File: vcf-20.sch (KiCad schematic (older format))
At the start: 51 parts, among them J1 IN1, J2 IN2, J3 POWER, J4 HP, J5 LP, J6 BP, J7 NOTCH, U1 TL072, U2 LM13700, U3 TL074, U4 TL074, U9 LM4040C5

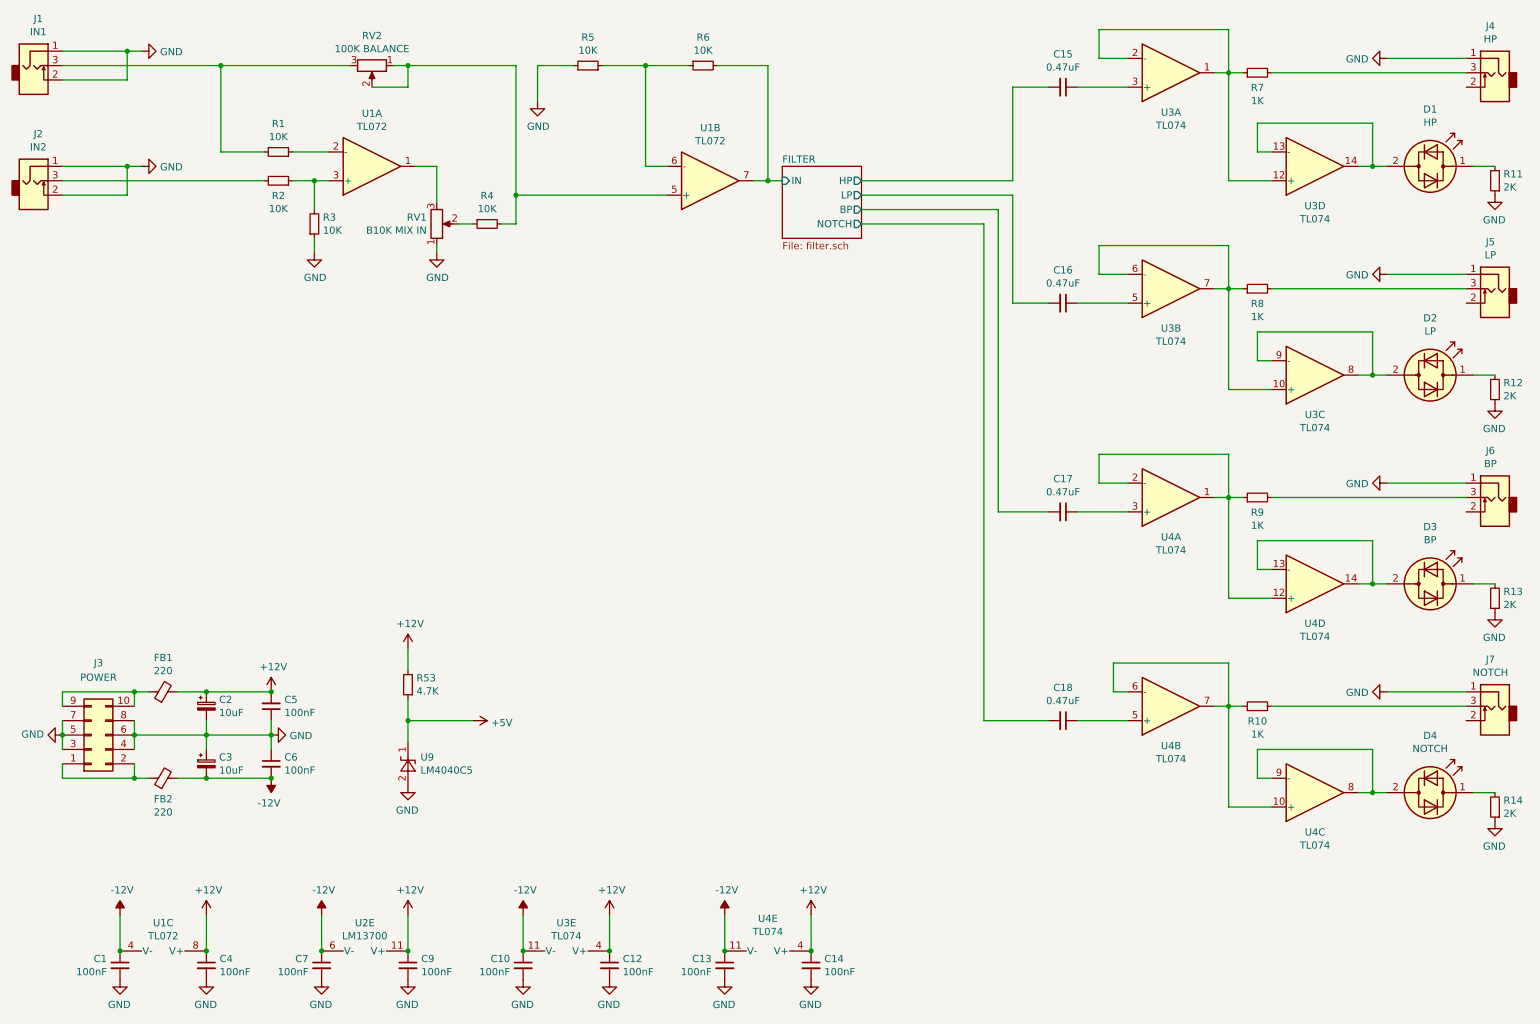
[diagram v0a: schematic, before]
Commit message: Update schematic with resonance and crossfader fixes
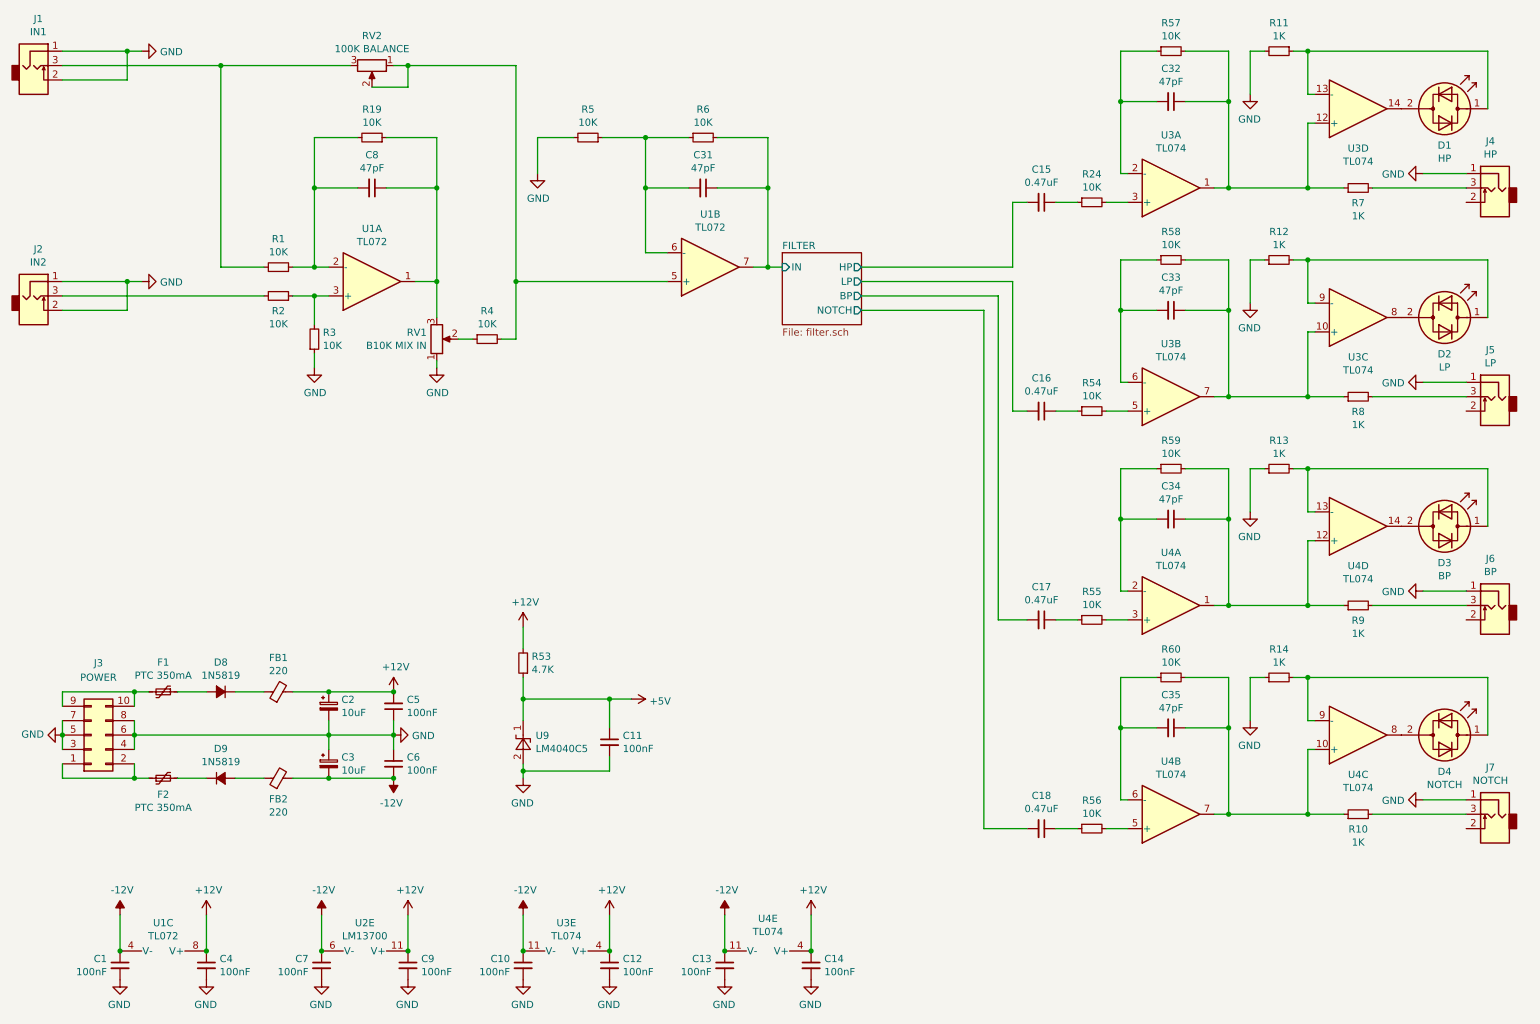
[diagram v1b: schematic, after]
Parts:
- added C11: 100nF, Capacitor_SMD:C_0603_1608Metric, symbol Device:C_Small
- added C31, C32, C33, C34, C35, C8: 47pF, Capacitor_SMD:C_0603_1608Metric, symbol Device:C_Small
- added D8, D9: 1N5819, symbol Device:D_Small_ALT
- added F1, F2: PTC 350mA, symbol Device:Polyfuse_Small
- added R19, R24, R54, R55, R56, R57, R58, R59, R60: 10K, Resistor_SMD:R_0603_1608Metric, symbol Device:R_Small
- R11, R12, R13, R14: value 2K -> 1K
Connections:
- net +5V: now also C11.1
- net FILTER/IN: now also C31.1
- net GND: now also R11.2, C11.2; no longer R11.1
- net at D1.1 (KA): now also R11.1, U3.13 (-); no longer R11.2
- net at D1.2 (AK), U3.14: no longer U3.13 (-)
- net at R7.1, U3.1, U3.12 (+): now also C32.1, R57.2; no longer U3.2 (-)
- net at J3.1 (Pin_1), J3.2 (Pin_2): now also F2.1; no longer FB2.1
- net at J3.10 (Pin_10), J3.9 (Pin_9): now also F1.2; no longer FB1.1
- net at U3.3 (+): now also R24.2; no longer C15.1
- net at R5.1, R6.1, U1.6 (-): now also C31.2
- net at D2.1 (KA), R12.2: now also U3.9 (-)
- net at D2.2 (AK), U3.8: no longer U3.9 (-)
- net at R8.1, U3.10 (+), U3.7: now also C33.1, R58.2; no longer U3.6 (-)
- net at U3.5 (+): now also R54.2; no longer C16.1
- net at D3.1 (KA), R13.2: now also U4.13 (-)
- net at D3.2 (AK), U4.14: no longer U4.13 (-)
- net at R9.1, U4.1, U4.12 (+): now also C34.1, R59.2; no longer U4.2 (-)
- net at U4.3 (+): now also R55.2; no longer C17.1
- net at R10.1, U4.10 (+), U4.7: now also C35.1, R60.2; no longer U4.6 (-)
- net at U4.5 (+): now also R56.2; no longer C18.1
- net at D4.1 (KA), R14.2: now also U4.9 (-)
- net at D4.2 (AK), U4.8: no longer U4.9 (-)
- net at RV1.3, U1.1: now also C8.1, R19.1
- net at R1.1, U1.2 (-): now also C8.2, R19.2
- new net: D8.1 (K), FB1.1
- new net: D9.2 (A), FB2.1
- new net: C32.2, R57.1, U3.2 (-)
- new net: C33.2, R58.1, U3.6 (-)
- new net: C34.2, R59.1, U4.2 (-)
- new net: C35.2, R60.1, U4.6 (-)
- new net: C17.1, R55.1
- new net: C16.1, R54.1
- new net: C15.1, R24.1
- new net: C18.1, R56.1
- new net: D8.2 (A), F1.1
- new net: D9.1 (K), F2.2
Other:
- moved on the sheet: C15, C16, C17, C18, C2, C3, C5, C6, D1, D2, D3, D4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

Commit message: Redesign filter core and revise board layout
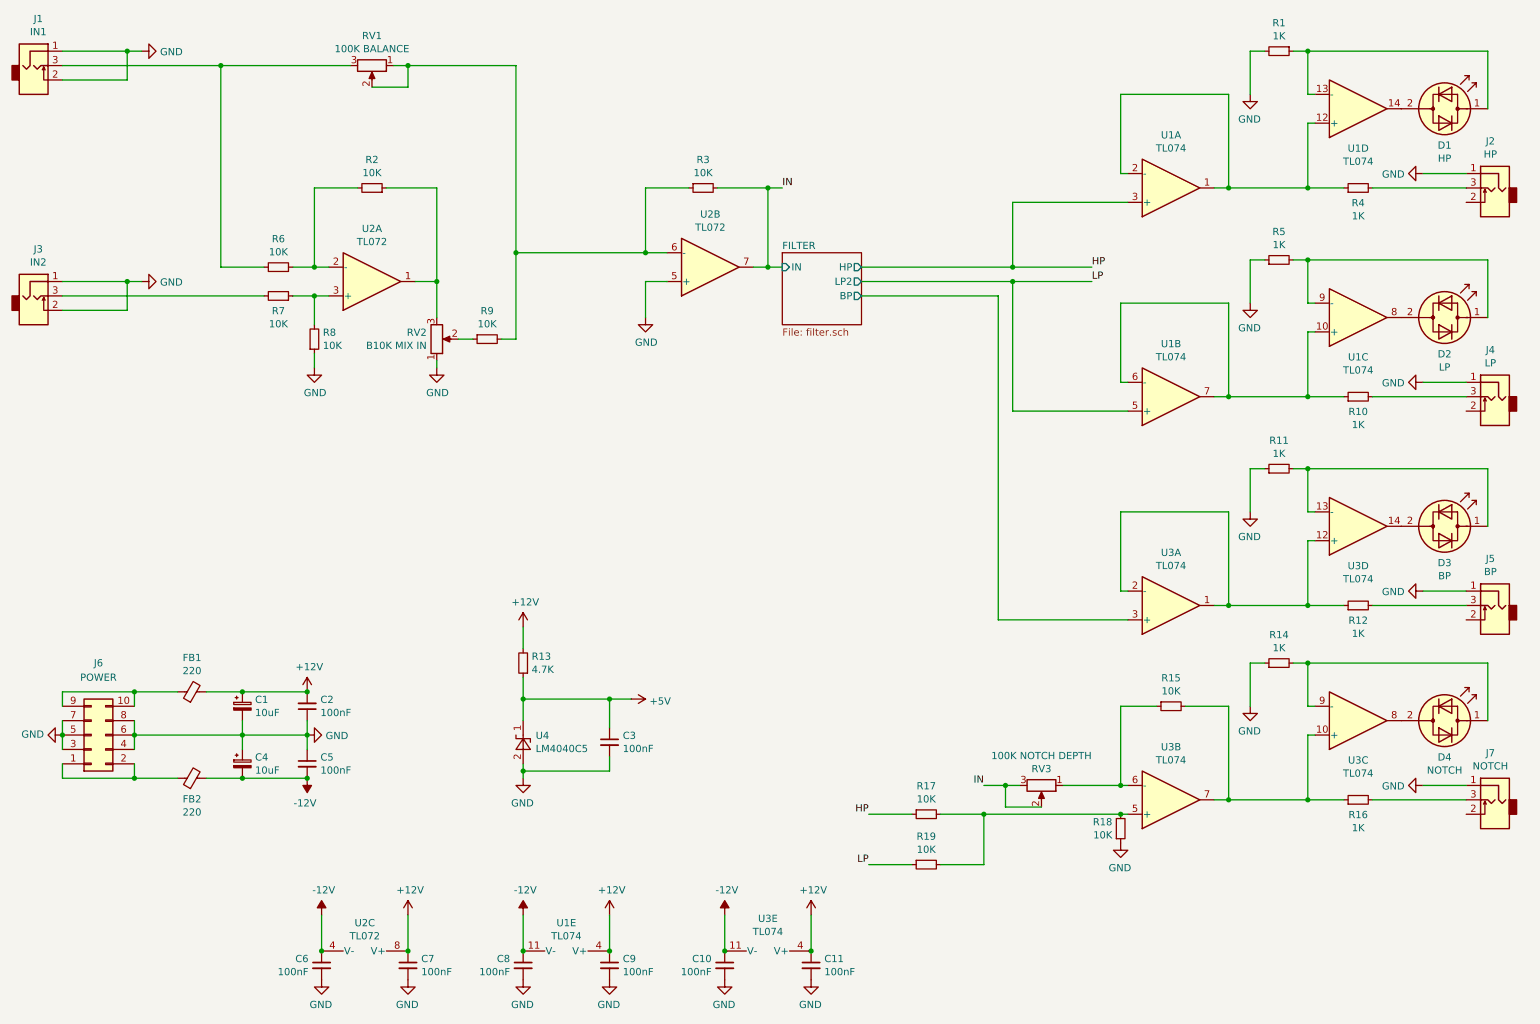
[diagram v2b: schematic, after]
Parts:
- removed C15, C16, C17, C18: 0.47uF, Capacitor_SMD:C_0603_1608Metric, symbol Device:C_Small
- removed C31, C32, C33, C34, C35, C8: 47pF, Capacitor_SMD:C_0603_1608Metric, symbol Device:C_Small
- removed C7, C9: 100nF, Capacitor_SMD:C_0603_1608Metric, symbol Device:C_Small
- removed D8, D9: 1N5819, symbol Device:D_Small_ALT
- removed F1, F2: PTC 350mA, symbol Device:Polyfuse_Small
- removed R24, R5, R54, R55, R57, R58, R59: 10K, Resistor_SMD:R_0603_1608Metric, symbol Device:R_Small
- removed U2: LM13700, Package_SO:SOIC-16_3.9x9.9mm_P1.27mm, symbol Amplifier_Operational:LM13700
- added R17, R18: 10K, Resistor_SMD:R_0603_1608Metric, symbol Device:R_Small
- added RV3: 100K NOTCH DEPTH, Potentiometer_SMD:Potentiometer_Bourns_TC33X_Vertical, symbol Device:R_POT
- renumbered C2 to C1, C13 to C10, C14 to C11, C5 to C2, C11 to C3, C3 to C4, C6 to C5, C1 to C6, C4 to C7, C10 to C8, C12 to C9, J4 to J2, J2 to J3, J5 to J4, J6 to J5, J3 to J6, R11 to R1, R8 to R10, R13 to R11, R9 to R12, R53 to R13, R60 to R15, R10 to R16, R56 to R19, R19 to R2, R6 to R3, R7 to R4, R12 to R5, R1 to R6, R2 to R7, R3 to R8, R4 to R9, RV2 to RV1, RV1 to RV2, U3 to U1, U1 to U2, U4 to U3, U9 to U4
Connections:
- net FILTER/BP: now also U3.3 (+)
- net GND: now also U2.5 (+), R18.1
- net at R4.1, U1.1, U1.12 (+): now also U1.2 (-)
- net at J6.1 (Pin_1), J6.2 (Pin_2): now also FB2.1
- net at J6.10 (Pin_10), J6.9 (Pin_9): now also FB1.1
- net HP: now reaches U1.3 (+)
- net HP: now also R17.1
- net at R9.2, RV1.1, RV1.2: now also R3.1, U2.6 (-); no longer U2.5 (+)
- net at R10.1, U1.10 (+), U1.7: now also U1.6 (-)
- net LP: now reaches U1.5 (+)
- net LP: now also R19.1
- net at R12.1, U3.1, U3.12 (+): now also U3.2 (-)
- net at R19.2, U3.5 (+): now also R17.2, R18.2
- net at R15.1, U3.6 (-): now also RV3.1
- net FILTER/IN renamed IN
- net IN: now also RV3.2, RV3.3
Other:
- moved on the sheet: C1, C2, C4, C5, C6, C7, D4, FB1, FB2, J7, R14, R15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
